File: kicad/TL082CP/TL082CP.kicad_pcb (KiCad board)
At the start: 2 copper layers, 88.6 x 75.4 mm, 18 parts, among them J1 AudioJack2_Switch, J2 AudioJack2_Switch, J3 PJ-102A, U1 TMR_1-1222, U2 TL082

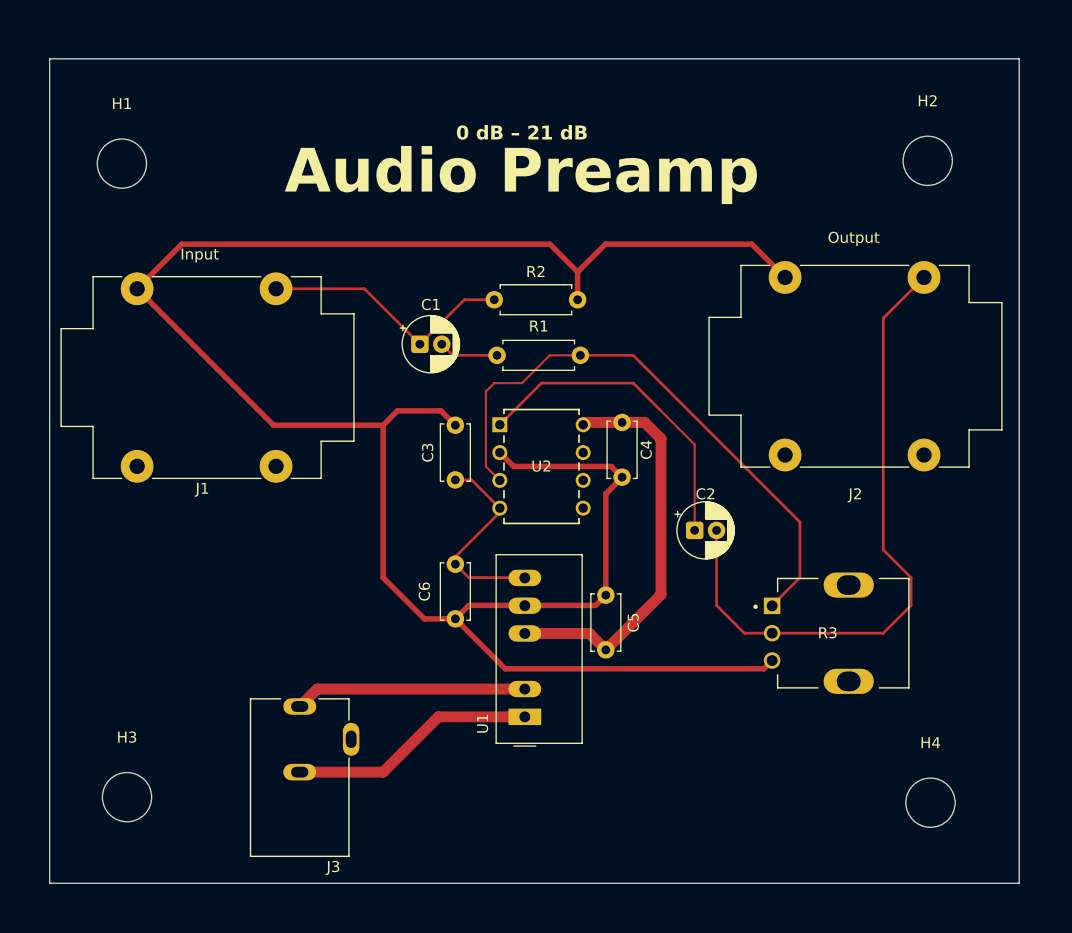
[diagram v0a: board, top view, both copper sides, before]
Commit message: fix: align mounting holes
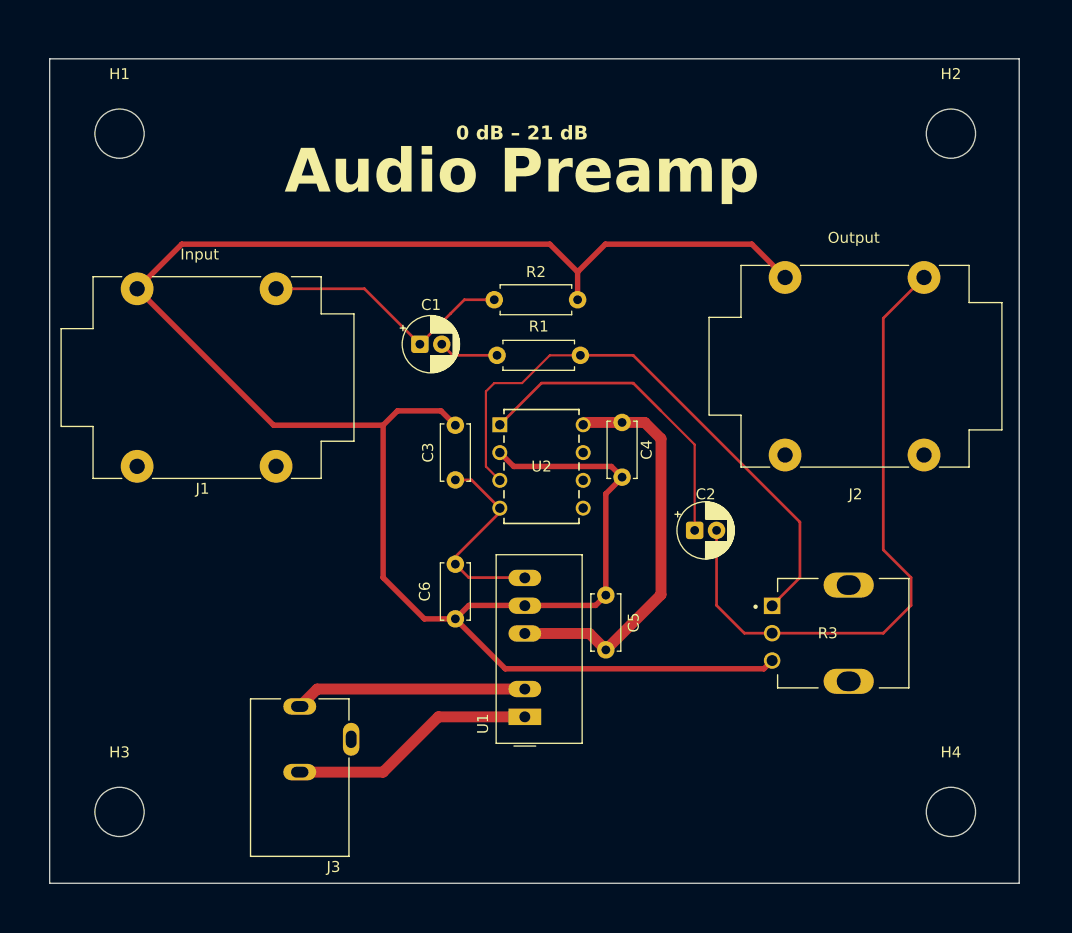
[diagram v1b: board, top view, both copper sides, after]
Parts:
- moved H2 3.27 mm to (177.0, 60.0)
- moved H1 2.75 mm to (101.0, 60.0)
- moved H4 2.05 mm to (177.0, 122.0)
- moved H3 1.52 mm to (101.0, 122.0)
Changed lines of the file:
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@@
 		(locked yes)
 		(layer "F.Cu")
-		(at 175.133 121.158)
+		(at 177 122)
 		(descr "Mounting Hole 4.5mm, no annular, generated by kicad-footprint-generator mountinghole.py")
 		(tags "mountinghole")
@@
 		(locked yes)
 		(layer "F.Cu")
-		(at 101.219 62.738)
+		(at 101 60)
 		(descr "Mounting Hole 4.5mm, no annular, generated by kicad-footprint-generator mountinghole.py")
 		(tags "mountinghole")
@@
 		(locked yes)
 		(layer "F.Cu")
-		(at 101.688 120.65)
+		(at 101 122)
 		(descr "Mounting Hole 4.5mm, no annular, generated by kicad-footprint-generator mountinghole.py")
 		(tags "mountinghole")
@@
 		(locked yes)
 		(layer "F.Cu")
-		(at 174.879 62.484)
+		(at 177 60)
 		(descr "Mounting Hole 4.5mm, no annular, generated by kicad-footprint-generator mountinghole.py")
 		(tags "mountinghole")

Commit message: fix(kicad): move ground plane from User.1 to B.Cu layer
The ground plane zone was incorrectly placed on User.1 documentation
layer instead of B.Cu copper layer. Added README section explaining
proper ground plane creation workflow for future reference.
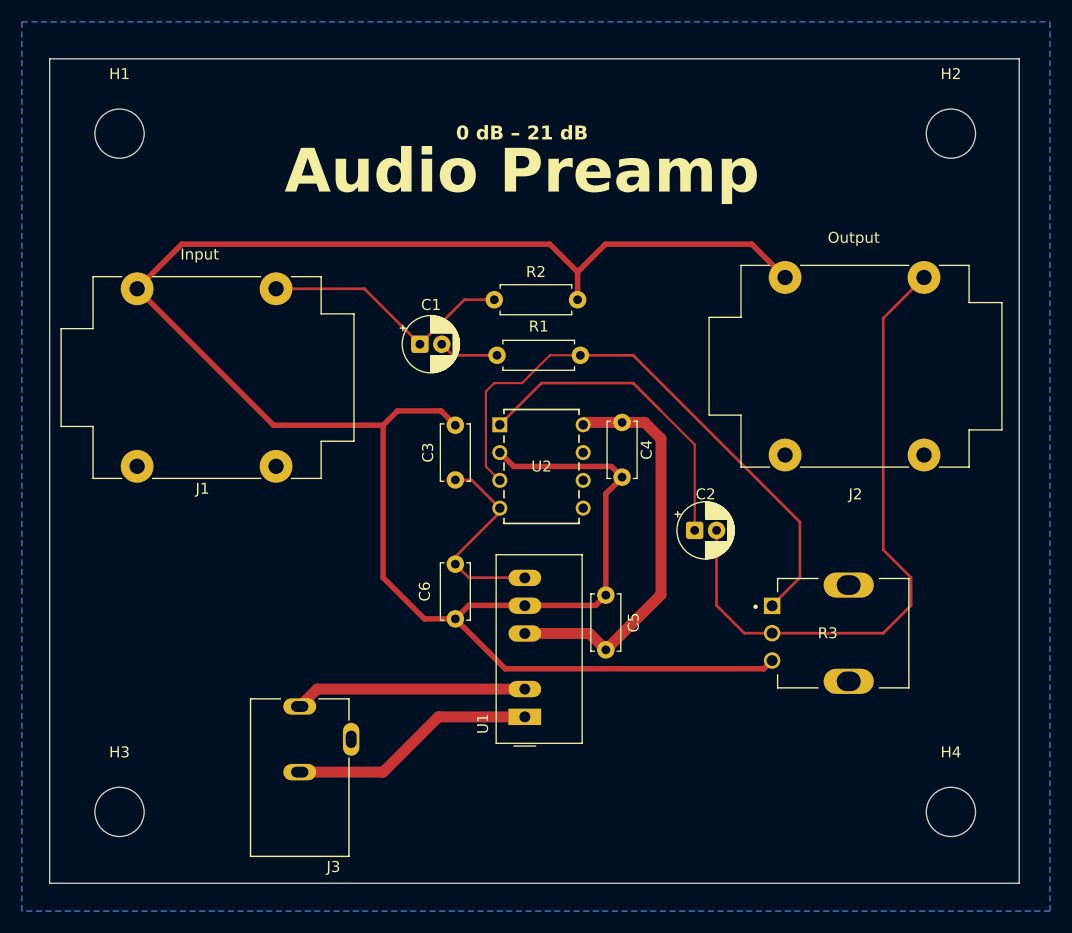
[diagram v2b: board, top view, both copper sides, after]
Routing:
- added copper zone on B.Cu, net GND
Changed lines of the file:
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@@
 	)
 	(zone
-		(net 0)
-		(net_name "")
-		(layer "User.1")
-		(name "Ground Plane")
+		(net 1)
+		(net_name "GND")
+		(layer "B.Cu")
 		(hatch edge 0.5)
 		(connect_pads
@@
 		(min_thickness 0.25)
 		(filled_areas_thickness no)
-		(fill
+		(fill yes
 			(thermal_gap 0.5)
 			(thermal_bridge_width 0.5)
@@
 		(polygon
 			(pts
-				(xy 94.615 52.324) (xy 183.515 52.324) (xy 183.515 128.524) (xy 94.615 128.524)
+				(xy 186.055 131.064) (xy 92.075 131.064) (xy 92.075 49.784) (xy 186.055 49.784)
 			)
 		)
